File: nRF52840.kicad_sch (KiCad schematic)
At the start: 22 parts, among them J3 JTAG_TC2030, J4 RGB, Q2 2N7002, Q3 AO3407, SW29 RESET, U4 MS88SF3

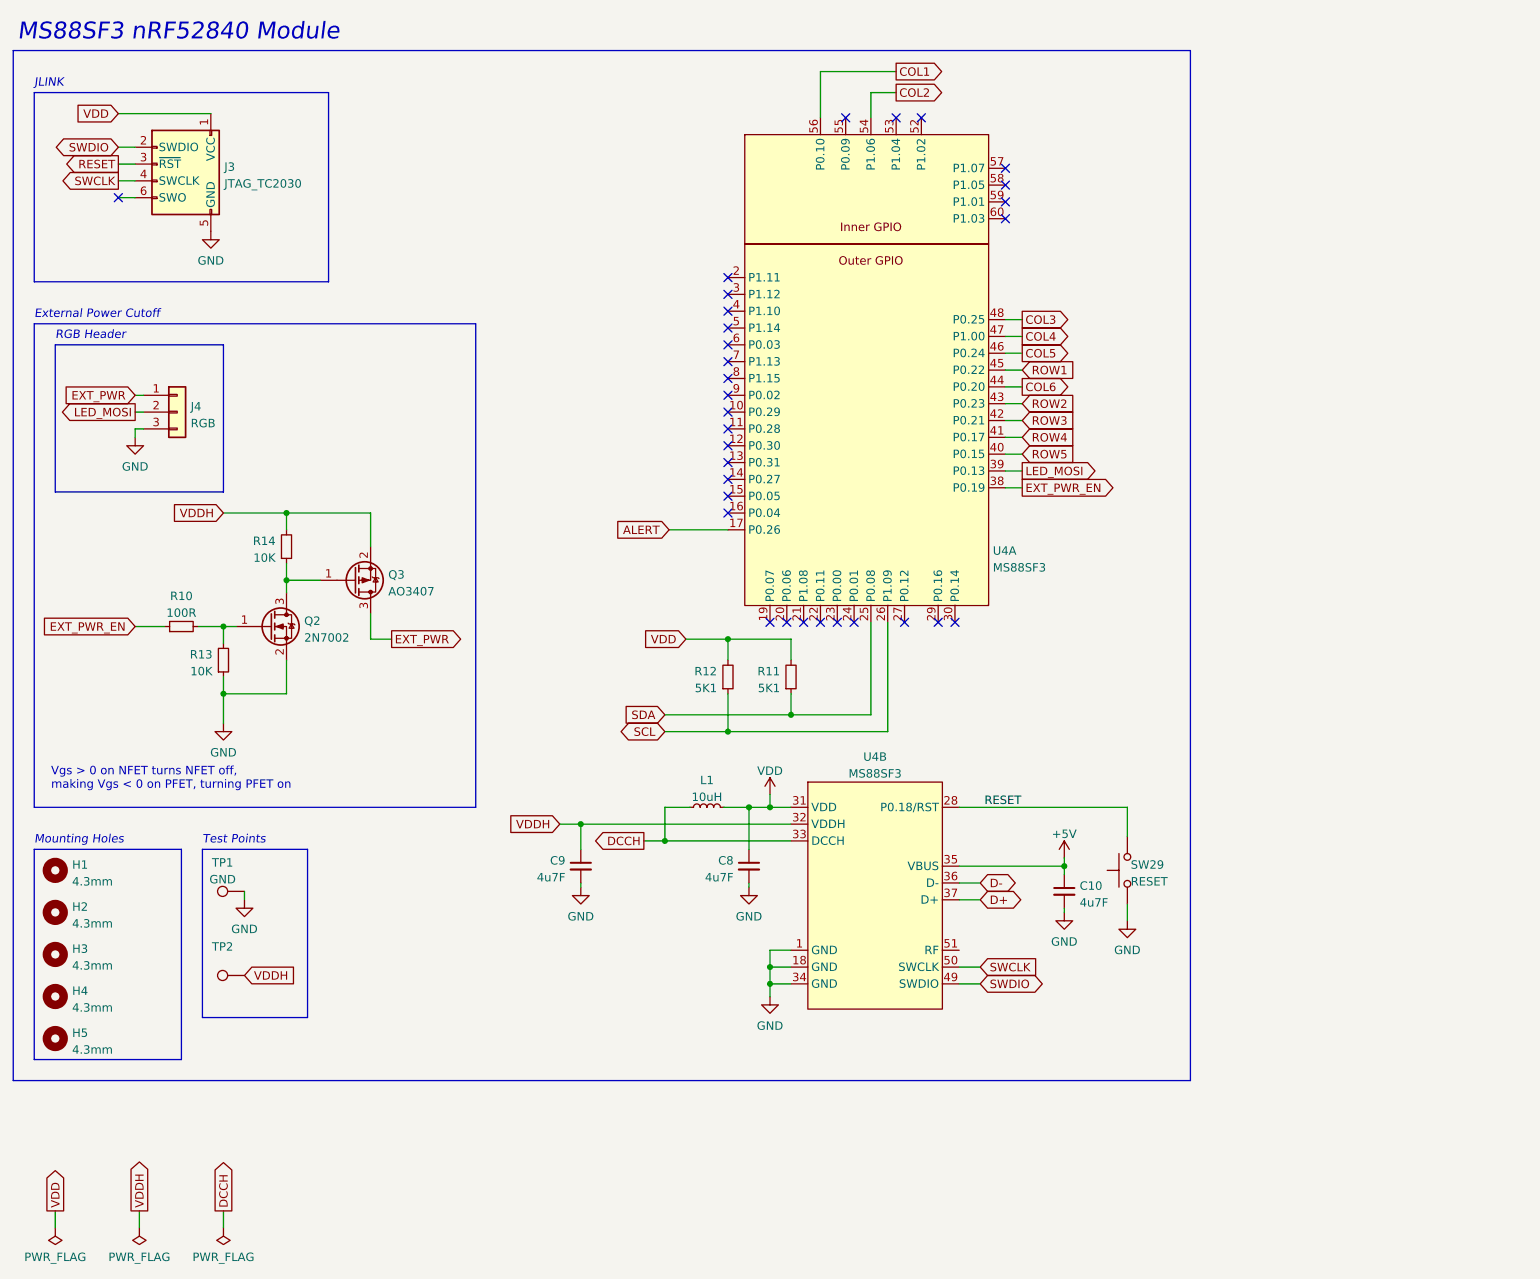
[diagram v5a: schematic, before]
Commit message: feat(pcb): Switch from 4.3mm NPTH mounting holes to M2 PTH
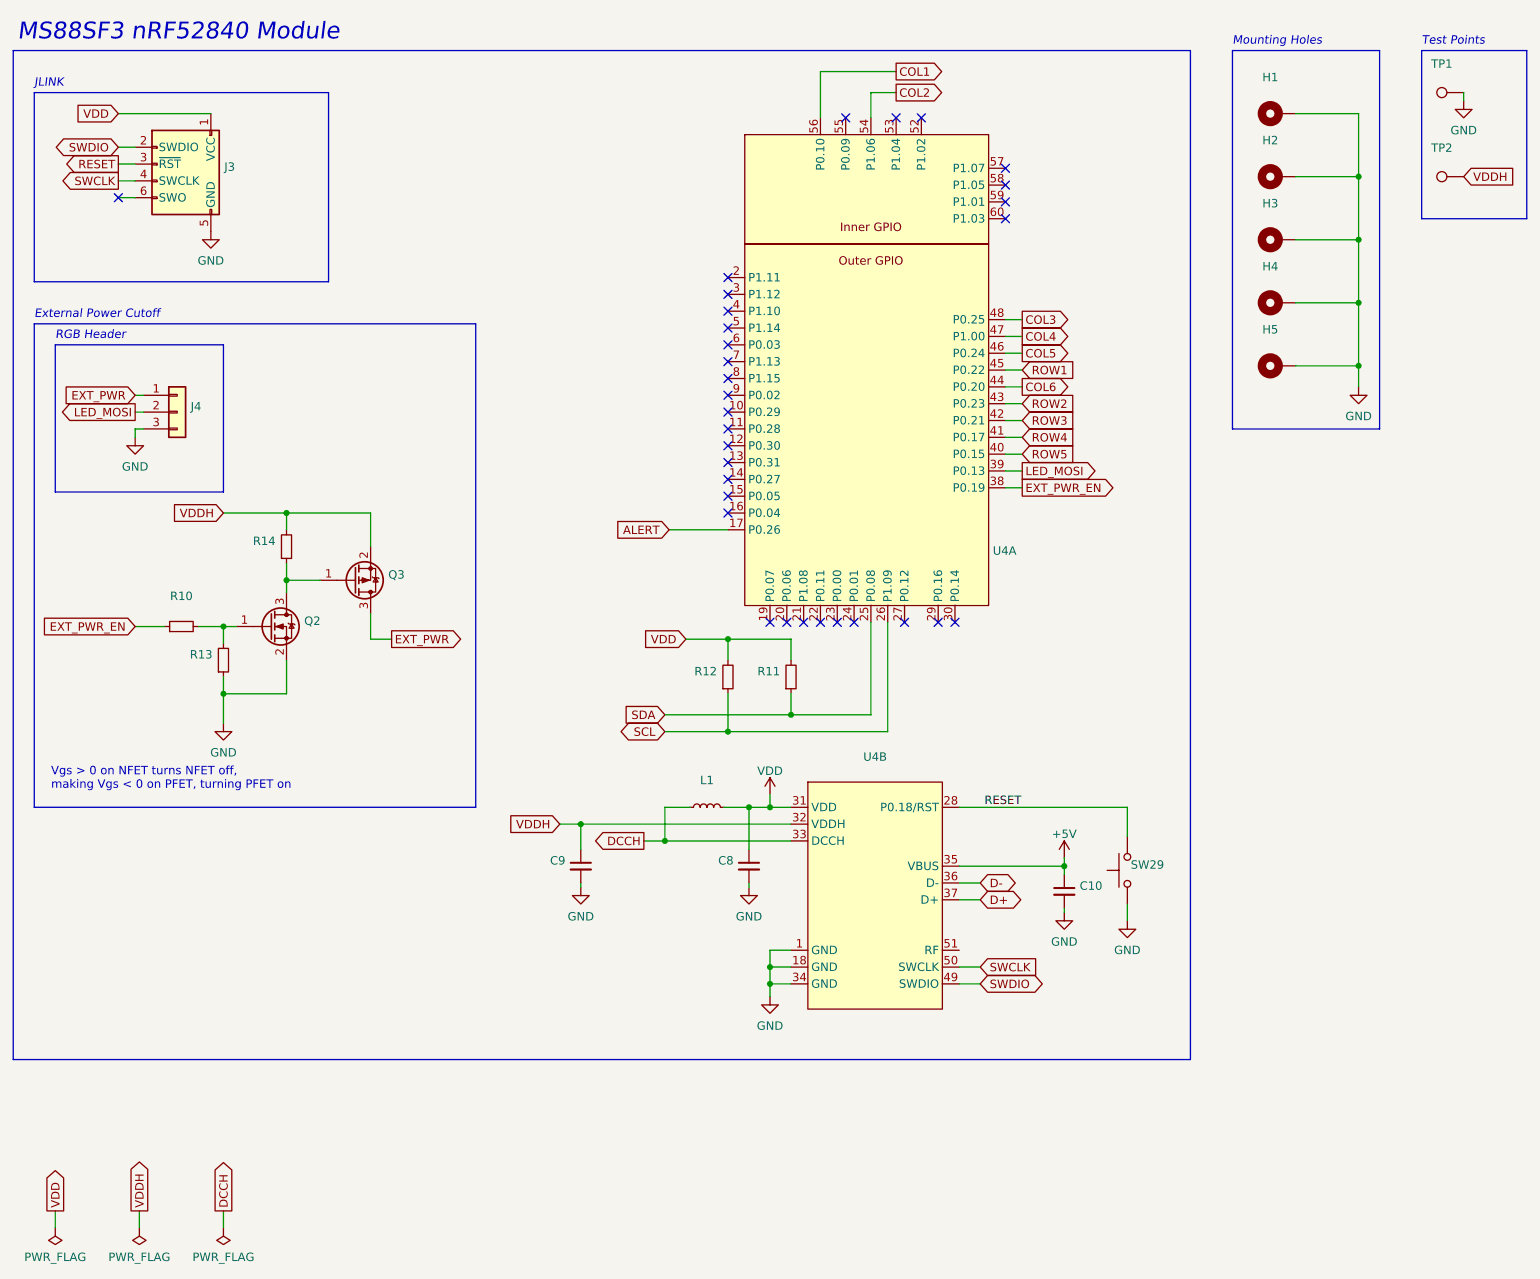
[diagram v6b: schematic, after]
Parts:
- removed H1, H2, H3, H4, H5: 4.3mm, Conejo:MountingHole_4.3mm, symbol Mechanical:MountingHole
- added H1, H2, H3, H4, H5: (no value), symbol Mechanical:MountingHole_Pad
- C10, C8, C9: value 4u7F -> (none); footprint Capacitor_SMD:C_0402_1005Metric -> (none)
- J3: value JTAG_TC2030 -> (none); footprint marbastlib-various:CON_TC2030_outlined -> (none)
- J4: value RGB -> (none); footprint Conejo:LED Header -> (none)
- L1: value 10uH -> (none); footprint Inductor_SMD:L_0603_1608Metric -> (none)
- Q2: value 2N7002 -> (none); footprint Package_TO_SOT_SMD:SOT-23 -> (none)
- Q3: value AO3407 -> (none); footprint Package_TO_SOT_SMD:SOT-23 -> (none)
- R10: value 100R -> (none); footprint Resistor_SMD:R_0402_1005Metric -> (none)
- R11, R12: value 5K1 -> (none); footprint Resistor_SMD:R_0603_1608Metric -> (none)
- R13, R14: value 10K -> (none); footprint Resistor_SMD:R_0402_1005Metric -> (none)
- SW29: value RESET -> (none); footprint Conejo:Panasonic_EVQPUL_EVQPUC (Reversible) -> (none)
- TP1: value GND -> (none); footprint TestPoint:TestPoint_THTPad_1.0x1.0mm_Drill0.5mm -> (none)
- U4: value MS88SF3 -> (none); footprint Conejo:MS88SF3_V2 -> (none)
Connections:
- net GND: now also H1.1, H2.1, H3.1, H4.1, H5.1
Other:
- moved on the sheet: TP1, TP2

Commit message: feat(pcb): Version 1.0.0
- Change decoupling capacitors from 4.7uF/1uF pairs to both 4.7uF
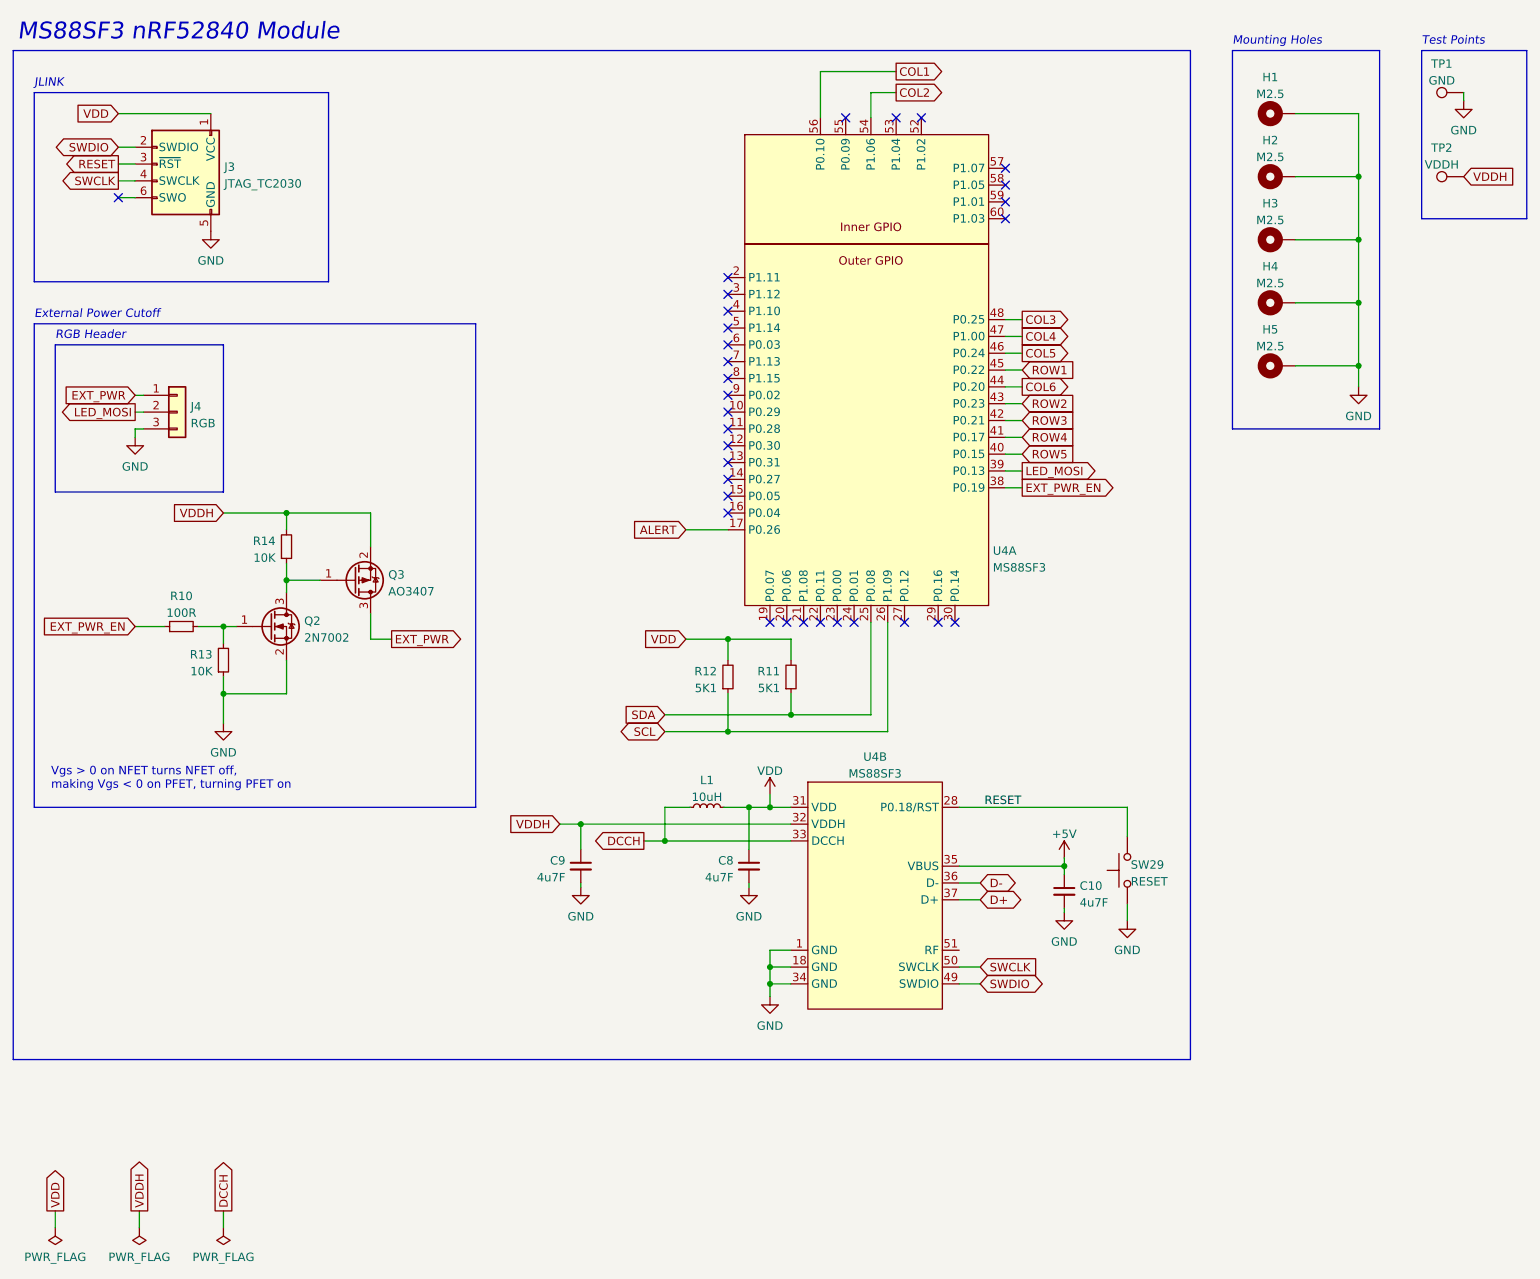
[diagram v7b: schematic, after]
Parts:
- C10, C8, C9: value (none) -> 4u7F; footprint (none) -> Capacitor_SMD:C_0402_1005Metric
- H1, H2, H3, H4, H5: value (none) -> M2.5; footprint (none) -> MountingHole:MountingHole_2.7mm_Pad_Via
- J3: value (none) -> JTAG_TC2030; footprint (none) -> marbastlib-various:CON_TC2030_outlined
- J4: value (none) -> RGB; footprint (none) -> Conejo:LED Header
- L1: value (none) -> 10uH; footprint (none) -> Inductor_SMD:L_0603_1608Metric
- Q2: value (none) -> 2N7002; footprint (none) -> Package_TO_SOT_SMD:SOT-23
- Q3: value (none) -> AO3407; footprint (none) -> Package_TO_SOT_SMD:SOT-23
- R10: value (none) -> 100R; footprint (none) -> Resistor_SMD:R_0402_1005Metric
- R11, R12: value (none) -> 5K1; footprint (none) -> Resistor_SMD:R_0603_1608Metric
- R13, R14: value (none) -> 10K; footprint (none) -> Resistor_SMD:R_0402_1005Metric
- SW29: value (none) -> RESET; footprint (none) -> Conejo:Panasonic_EVQPUL_EVQPUC (Reversible)
- TP1: value (none) -> GND; footprint (none) -> TestPoint:TestPoint_THTPad_1.0x1.0mm_Drill0.5mm
- TP2: value (none) -> VDDH; footprint (none) -> TestPoint:TestPoint_Pad_D1.0mm
- U4: value (none) -> MS88SF3; footprint (none) -> Conejo:MS88SF3_V2
